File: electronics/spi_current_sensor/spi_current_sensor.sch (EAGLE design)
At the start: 3 parts, among them J2 METALTEX-2, U1 TLI4970_D025T5

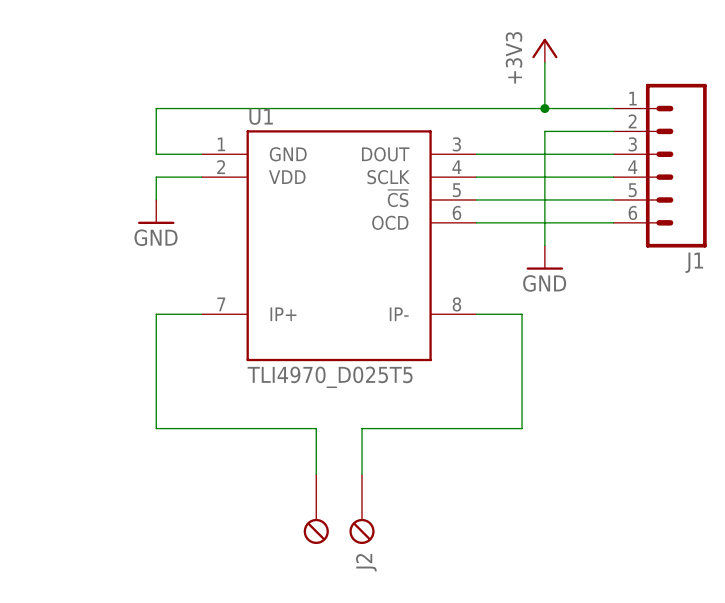
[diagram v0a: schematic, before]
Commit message: Add decoupler capacitor to current sensor
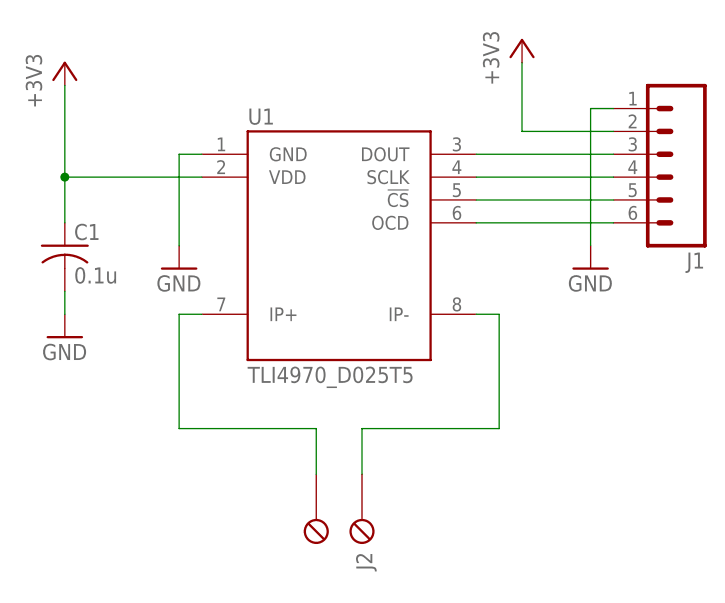
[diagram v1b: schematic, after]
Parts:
- added C1: 0.1u, adafruit:C-US025-025X050
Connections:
- net +3V3: now also C1.1, J1.2, U1.VDD; no longer J1.1, U1.GND
- net GND: now also C1.2, J1.1, U1.GND; no longer J1.2, U1.VDD
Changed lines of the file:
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@@
 <drawing>
 <settings>
-<setting alwaysvectorfont="no"/>
+<setting alwaysvectorfont="yes"/>
 <setting verticaltext="up"/>
 </settings>
@@
 <part name="U1" library="uchile_robotics_eagle_lib" deviceset="TLI4970_D025T5" device=""/>
 <part name="J1" library="uchile_robotics_eagle_lib" deviceset="M06" device="LONGPADS"/>
-<part name="+3V1" library="supply1" deviceset="+3V3" device=""/>
+<part name="J2" library="uchile_robotics_eagle_lib" deviceset="METALTEX-2" device=""/>
+<part name="C1" library="adafruit" deviceset="C-US" device="025-025X050" value="0.1u"/>
+<part name="GND3" library="supply1" deviceset="GND" device=""/>
+<part name="GND2" library="supply1" deviceset="GND" device=""/>
+<part name="+3V2" library="supply1" deviceset="+3V3" device=""/>
 <part name="GND1" library="supply1" deviceset="GND" device=""/>
-<part name="GND2" library="supply1" deviceset="GND" device=""/>
-<part name="J2" library="uchile_robotics_eagle_lib" deviceset="METALTEX-2" device=""/>
+<part name="+3V3" library="supply1" deviceset="+3V3" device=""/>
 </parts>
 <sheets>
@@
 <instance part="U1" gate="G$1" x="20.32" y="60.96"/>
 <instance part="J1" gate="G$1" x="55.88" y="71.12" rot="R180"/>
-<instance part="+3V1" gate="G$1" x="43.18" y="83.82"/>
-<instance part="GND1" gate="1" x="43.18" y="58.42"/>
-<instance part="GND2" gate="1" x="0" y="63.5"/>
 <instance part="J2" gate="G$1" x="22.86" y="27.94" rot="R270"/>
+<instance part="C1" gate="G$1" x="-10.16" y="60.96"/>
+<instance part="GND3" gate="1" x="-10.16" y="50.8"/>
+<instance part="GND2" gate="1" x="2.54" y="58.42"/>
+<instance part="+3V2" gate="G$1" x="-10.16" y="81.28"/>
+<instance part="GND1" gate="1" x="48.26" y="58.42"/>
+<instance part="+3V3" gate="G$1" x="40.64" y="83.82"/>
 </instances>
 <busses>
 </busses>
 <nets>
-<net name="+3V3" class="0">
+<net name="GND" class="0">
+<segment>
+<pinref part="U1" gate="G$1" pin="GND"/>
+<pinref part="GND2" gate="1" pin="GND"/>
+<wire x1="5.08" y1="71.12" x2="2.54" y2="71.12" width="0.1524" layer="91"/>
+<wire x1="2.54" y1="71.12" x2="2.54" y2="60.96" width="0.1524" layer="91"/>
+</segment>
+<segment>
+<pinref part="GND3" gate="1" pin="GND"/>
+<pinref part="C1" gate="G$1" pin="2"/>
+<wire x1="-10.16" y1="53.34" x2="-10.16" y2="55.88" width="0.1524" layer="91"/>
+</segment>
 <segment>
 <pinref part="J1" gate="G$1" pin="1"/>
-<pinref part="+3V1" gate="G$1" pin="+3V3"/>
-<wire x1="50.8" y1="76.2" x2="43.18" y2="76.2" width="0.1524" layer="91"/>
-<wire x1="43.18" y1="76.2" x2="43.18" y2="81.28" width="0.1524" layer="91"/>
-<wire x1="43.18" y1="76.2" x2="0" y2="76.2" width="0.1524" layer="91"/>
-<wire x1="0" y1="76.2" x2="0" y2="71.12" width="0.1524" layer="91"/>
-<pinref part="U1" gate="G$1" pin="GND"/>
-<wire x1="0" y1="71.12" x2="5.08" y2="71.12" width="0.1524" layer="91"/>
-<junction x="43.18" y="76.2"/>
-</segment>
-</net>
-<net name="GND" class="0">
-<segment>
-<pinref part="J1" gate="G$1" pin="2"/>
 <pinref part="GND1" gate="1" pin="GND"/>
-<wire x1="50.8" y1="73.66" x2="43.18" y2="73.66" width="0.1524" layer="91"/>
-<wire x1="43.18" y1="73.66" x2="43.18" y2="60.96" width="0.1524" layer="91"/>
-</segment>
-<segment>
-<pinref part="U1" gate="G$1" pin="VDD"/>
-<pinref part="GND2" gate="1" pin="GND"/>
-<wire x1="5.08" y1="68.58" x2="0" y2="68.58" width="0.1524" layer="91"/>
-<wire x1="0" y1="68.58" x2="0" y2="66.04" width="0.1524" layer="91"/>
+<wire x1="50.8" y1="76.2" x2="48.26" y2="76.2" width="0.1524" layer="91"/>
+<wire x1="48.26" y1="76.2" x2="48.26" y2="60.96" width="0.1524" layer="91"/>
 </segment>
 </net>
@@
 <pinref part="J2" gate="G$1" pin="P2"/>
 <wire x1="17.78" y1="35.56" x2="17.78" y2="40.64" width="0.1524" layer="91"/>
-<wire x1="17.78" y1="40.64" x2="0" y2="40.64" width="0.1524" layer="91"/>
-<wire x1="0" y1="40.64" x2="0" y2="53.34" width="0.1524" layer="91"/>
+<wire x1="17.78" y1="40.64" x2="2.54" y2="40.64" width="0.1524" layer="91"/>
+<wire x1="2.54" y1="40.64" x2="2.54" y2="53.34" width="0.1524" layer="91"/>
 <pinref part="U1" gate="G$1" pin="IP+"/>
-<wire x1="0" y1="53.34" x2="5.08" y2="53.34" width="0.1524" layer="91"/>
+<wire x1="2.54" y1="53.34" x2="5.08" y2="53.34" width="0.1524" layer="91"/>
 </segment>
 </net>
@@
 <pinref part="J2" gate="G$1" pin="P1"/>
 <wire x1="22.86" y1="35.56" x2="22.86" y2="40.64" width="0.1524" layer="91"/>
-<wire x1="22.86" y1="40.64" x2="40.64" y2="40.64" width="0.1524" layer="91"/>
-<wire x1="40.64" y1="40.64" x2="40.64" y2="53.34" width="0.1524" layer="91"/>
+<wire x1="22.86" y1="40.64" x2="38.1" y2="40.64" width="0.1524" layer="91"/>
+<wire x1="38.1" y1="40.64" x2="38.1" y2="53.34" width="0.1524" layer="91"/>
 <pinref part="U1" gate="G$1" pin="IP-"/>
-<wire x1="40.64" y1="53.34" x2="35.56" y2="53.34" width="0.1524" layer="91"/>
-</segment>
-</net>
+<wire x1="38.1" y1="53.34" x2="35.56" y2="53.34" width="0.1524" layer="91"/>
+</segment>
+</net>
+<net name="+3V3" class="0">
+<segment>
+<pinref part="U1" gate="G$1" pin="VDD"/>
+<pinref part="+3V2" gate="G$1" pin="+3V3"/>
+<wire x1="5.08" y1="68.58" x2="-10.16" y2="68.58" width="0.1524" layer="91"/>
+<wire x1="-10.16" y1="68.58" x2="-10.16" y2="78.74" width="0.1524" layer="91"/>
+<pinref part="C1" gate="G$1" pin="1"/>
+<wire x1="-10.16" y1="63.5" x2="-10.16" y2="68.58" width="0.1524" layer="91"/>
+<junction x="-10.16" y="68.58"/>
+</segment>
+<segment>
+<pinref part="J1" gate="G$1" pin="2"/>
+<pinref part="+3V3" gate="G$1" pin="+3V3"/>
+<wire x1="50.8" y1="73.66" x2="40.64" y2="73.66" width="0.1524" layer="91"/>
+<wire x1="40.64" y1="73.66" x2="40.64" y2="81.28" width="0.1524" layer="91"/>
+</segment>
+</net>
